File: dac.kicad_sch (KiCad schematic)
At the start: 29 parts, among them U6 PCM5242RHBR, X1 22.5792Mhz, X2 24.576Mhz

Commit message: Page settings
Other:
- company: (none) -> github.com/pedalboard
- title: (none) -> Open Pedalboard Soundcard
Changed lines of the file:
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@@
 (kicad_sch (version 20230121) (generator eeschema)
   (paper "A4")
+  (title_block
+    (title "Open Pedalboard Soundcard")
+    (date "2023-12-19")
+    (rev "0.0.1")
+    (company "github.com/pedalboard")
+    (comment 1 "Source Code: https://github.com/pedalboard/pedalboard-hw")
+    (comment 2 "License: CERN Open Hardware Licence Version 2 - Permissive")
+  )
   (junction (at 99.06 73.66) (diameter 0) (color 0 0 0 0)
   )

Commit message: Distribute parts on PCB
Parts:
- added J2: Conn_02x03_Odd_Even, Connector_PinHeader_2.54mm:PinHeader_2x03_P2.54mm_Vertical, symbol Connector_Generic:Conn_02x03_Odd_Even
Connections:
- net GND: now also J2.3 (Pin_3), J2.4 (Pin_4)
- net outl+: now also J2.6 (Pin_6)
- net outl-: now also J2.5 (Pin_5)
- net outr+: now also J2.2 (Pin_2)
- net outr-: now also J2.1 (Pin_1)
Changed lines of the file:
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@@
+    (stroke (width 0) (type default))
+  )
+  (wire (pts (xy 59.69 139.7) (xy 53.34 139.7))
     (stroke (width 0) (type default))
   )
@@
     (stroke (width 0) (type default))
   )
-  (wire (pts (xy 45.72 137.16) (xy 46.99 137.16))
+  (wire (pts (xy 144.78 156.21) (xy 138.43 156.21))
+    (stroke (width 0) (type default))
+  )
+  (wire (pts (xy 39.37 137.16) (xy 46.99 137.16))
     (stroke (width 0) (type default))
   )
@@
     (stroke (width 0) (type default))
   )
+  (wire (pts (xy 144.78 161.29) (xy 138.43 161.29))
+    (stroke (width 0) (type default))
+  )
   (wire (pts (xy 238.76 76.2) (xy 238.76 73.66))
     (stroke (width 0) (type default))
@@
     (stroke (width 0) (type default))
   )
+  (wire (pts (xy 113.03 158.75) (xy 125.73 158.75))
+    (stroke (width 0) (type default))
+  )
   (wire (pts (xy 71.12 161.29) (xy 77.47 161.29))
     (stroke (width 0) (type default))
@@
     (stroke (width 0) (type default))
   )
-  (wire (pts (xy 72.39 139.7) (xy 71.12 139.7))
-    (stroke (width 0) (type default))
-  )
   (wire (pts (xy 204.47 85.09) (xy 204.47 81.28))
     (stroke (width 0) (type default))
@@
     (stroke (width 0) (type default))
   )
-  (wire (pts (xy 78.74 137.16) (xy 77.47 137.16))
+  (wire (pts (xy 86.36 137.16) (xy 77.47 137.16))
     (stroke (width 0) (type default))
   )
@@
     (stroke (width 0) (type default))
   )
+  (wire (pts (xy 119.38 156.21) (xy 125.73 156.21))
+    (stroke (width 0) (type default))
+  )
   (wire (pts (xy 85.09 105.41) (xy 102.87 105.41))
     (stroke (width 0) (type default))
@@
     (stroke (width 0) (type default))
   )
-  (wire (pts (xy 52.07 139.7) (xy 53.34 139.7))
-    (stroke (width 0) (type default))
-  )
   (wire (pts (xy 148.59 100.33) (xy 170.18 100.33))
     (stroke (width 0) (type default))
@@
     (stroke (width 0) (type default))
   )
+  (wire (pts (xy 138.43 158.75) (xy 151.13 158.75))
+    (stroke (width 0) (type default))
+  )
+  (wire (pts (xy 64.77 139.7) (xy 71.12 139.7))
+    (stroke (width 0) (type default))
+  )
   (wire (pts (xy 191.77 92.71) (xy 191.77 102.87))
     (stroke (width 0) (type default))
@@
     (stroke (width 0) (type default))
   )
+  (wire (pts (xy 119.38 161.29) (xy 125.73 161.29))
+    (stroke (width 0) (type default))
+  )
   (wire (pts (xy 53.34 161.29) (xy 53.34 154.94))
     (stroke (width 0) (type default))
@@
   (wire (pts (xy 182.88 102.87) (xy 182.88 110.49))
     (stroke (width 0) (type default))
+  )
+  (label "outl-" (at 59.69 139.7 180) (fields_autoplaced)
+    (effects (font (size 1.27 1.27)) (justify right bottom))
+  )
+  (label "outl+" (at 144.78 161.29 180) (fields_autoplaced)
+    (effects (font (size 1.27 1.27)) (justify right bottom))
+  )
+  (label "outl-" (at 119.38 161.29 0) (fields_autoplaced)
+    (effects (font (size 1.27 1.27)) (justify left bottom))
+  )
+  (label "outr+" (at 86.36 137.16 180) (fields_autoplaced)
+    (effects (font (size 1.27 1.27)) (justify right bottom))
+  )
+  (label "outr-" (at 119.38 156.21 0) (fields_autoplaced)
+    (effects (font (size 1.27 1.27)) (justify left bottom))
+  )
+  (label "outr+" (at 144.78 156.21 180) (fields_autoplaced)
+    (effects (font (size 1.27 1.27)) (justify right bottom))
+  )
+  (label "outl+" (at 39.37 137.16 0) (fields_autoplaced)
+    (effects (font (size 1.27 1.27)) (justify left bottom))
+  )
+  (label "outr-" (at 64.77 139.7 0) (fields_autoplaced)
+    (effects (font (size 1.27 1.27)) (justify left bottom))
   )
   (global_label "DVDD" (shape input) (at 95.25 73.66 180)
@@
     )
   )
-  (global_label "outr+" (shape input) (at 78.74 137.16 0)
-    (effects (font (size 1.27 1.27)) (justify left))
-    (property "Intersheetrefs" "${INTERSHEET_REFS}" (at 78.74 137.16 0)
-      (effects (font (size 1.27 1.27)) hide)
-    )
-  )
   (global_label "DIN" (shape input) (at 148.59 97.79 0)
     (effects (font (size 1.27 1.27)) (justify left))
     (property "Intersheetrefs" "${INTERSHEET_REFS}" (at 148.59 97.79 0)
-      (effects (font (size 1.27 1.27)) hide)
-    )
-  )
-  (global_label "outr-" (shape input) (at 72.39 139.7 0)
-    (effects (font (size 1.27 1.27)) (justify left))
-    (property "Intersheetrefs" "${INTERSHEET_REFS}" (at 72.39 139.7 0)
       (effects (font (size 1.27 1.27)) hide)
     )
@@
     )
   )
-  (global_label "outl-" (shape input) (at 52.07 139.7 180)
-    (effects (font (size 1.27 1.27)) (justify right))
-    (property "Intersheetrefs" "${INTERSHEET_REFS}" (at 52.07 139.7 0)
-      (effects (font (size 1.27 1.27)) hide)
-    )
-  )
   (global_label "AVDD" (shape input) (at 86.36 118.11 180)
     (effects (font (size 1.27 1.27)) (justify right))
     (property "Intersheetrefs" "${INTERSHEET_REFS}" (at 86.36 118.11 0)
-      (effects (font (size 1.27 1.27)) hide)
-    )
-  )
-  (global_label "outl+" (shape input) (at 45.72 137.16 180)
-    (effects (font (size 1.27 1.27)) (justify right))
-    (property "Intersheetrefs" "${INTERSHEET_REFS}" (at 45.72 137.16 0)
       (effects (font (size 1.27 1.27)) hide)
     )
@@
     )
   )
+  (symbol (lib_id "power:GND") (at 151.13 158.75 0) (unit 1)
+    (in_bom yes) (on_board yes) (dnp no) (fields_autoplaced)
+    (property "Reference" "#PWR017" (at 151.13 165.1 0)
+      (effects (font (size 1.27 1.27)) hide)
+    )
+    (property "Value" "GND" (at 151.13 163.83 0)
+      (effects (font (size 1.27 1.27)))
+    )
+    (property "Footprint" "" (at 151.13 158.75 0)
+      (effects (font (size 1.27 1.27)) hide)
+    )
+    (property "Datasheet" "" (at 151.13 158.75 0)
+      (effects (font (size 1.27 1.27)) hide)
+    )
+    (pin "1")
+    (instances
+      (project "pedalboard-soundcard"
+        (path "/257597c6-fbef-4478-b0f4-968f2d6f1866/c0100554-f979-4e8d-b08c-e48cc1e12bdc"
+          (reference "#PWR017") (unit 1)
+        )
+      )
+    )
+  )
+  (symbol (lib_id "power:GND") (at 113.03 158.75 0) (unit 1)
+    (in_bom yes) (on_board yes) (dnp no) (fields_autoplaced)
+    (property "Reference" "#PWR016" (at 113.03 165.1 0)
+      (effects (font (size 1.27 1.27)) hide)
+    )
+    (property "Value" "GND" (at 113.03 163.83 0)
+      (effects (font (size 1.27 1.27)))
+    )
+    (property "Footprint" "" (at 113.03 158.75 0)
+      (effects (font (size 1.27 1.27)) hide)
+    )
+    (property "Datasheet" "" (at 113.03 158.75 0)
+      (effects (font (size 1.27 1.27)) hide)
+    )
+    (pin "1")
+    (instances
+      (project "pedalboard-soundcard"
+        (path "/257597c6-fbef-4478-b0f4-968f2d6f1866/c0100554-f979-4e8d-b08c-e48cc1e12bdc"
+          (reference "#PWR016") (unit 1)
+        )
+      )
+    )
+  )
   (symbol (lib_id "power:GND") (at 152.4 83.82 0) (unit 1)
     (in_bom yes) (on_board yes) (dnp no)
@@
       (effects (font (size 1.524 1.524)) hide)
     )
-    (property "Datasheet" "" (at 102.87 85.09 0)
+    (property "Datasheet" "https://www.ti.com/lit/ds/symlink/pcm5242.pdf" (at 85.09 44.45 0)
       (effects (font (size 1.524 1.524)))
     )
@@
         )
       )
+    )
+  )
+  (symbol (lib_id "Connector_Generic:Conn_02x03_Odd_Even") (at 130.81 158.75 0) (unit 1)
+    (in_bom yes) (on_board yes) (dnp no) (fields_autoplaced)
+    (property "Reference" "J2" (at 132.08 149.86 0)
+      (effects (font (size 1.27 1.27)))
+    )
+    (property "Value" "Conn_02x03_Odd_Even" (at 132.08 152.4 0)
+      (effects (font (size 1.27 1.27)))
+    )
+    (property "Footprint" "Connector_PinHeader_2.54mm:PinHeader_2x03_P2.54mm_Vertical" (at 130.81 158.75 0)
+      (effects (font (size 1.27 1.27)) hide)
+    )
+    (property "Datasheet" "~" (at 130.81 158.75 0)
+      (effects (font (size 1.27 1.27)) hide)
+    )
+    (pin "1")
+    (pin "2")
+    (pin "3")
+    (pin "4")
+    (pin "5")
+    (pin "6")
+    (instances
+      (project "pedalboard-soundcard"
+        (path "/257597c6-fbef-4478-b0f4-968f2d6f1866/c0100554-f979-4e8d-b08c-e48cc1e12bdc"
+          (reference "J2") (unit 1)
+        )
+      )

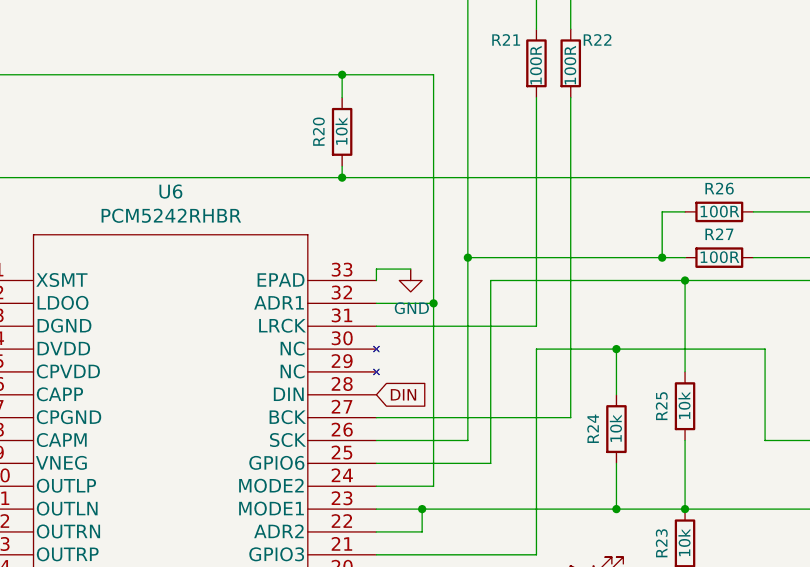
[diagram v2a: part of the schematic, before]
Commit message: First routing attempt
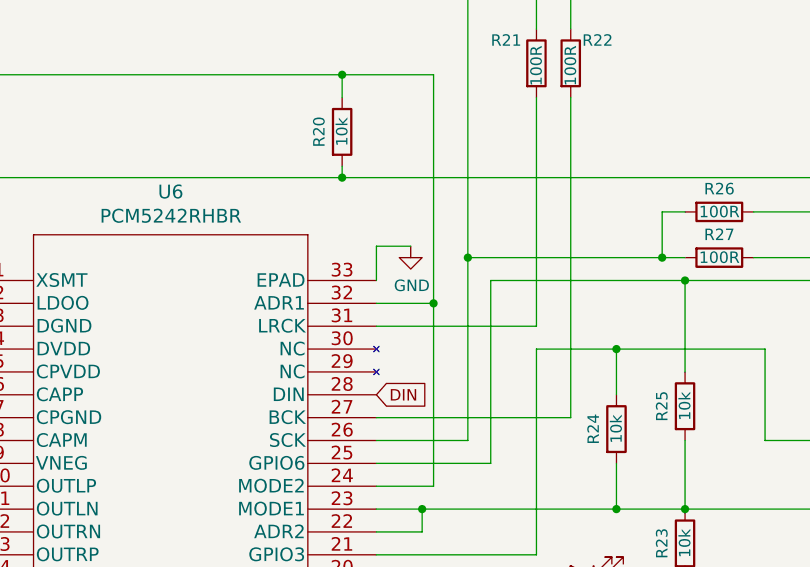
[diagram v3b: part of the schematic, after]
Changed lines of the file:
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@@
     (stroke (width 0) (type default))
   )
-  (wire (pts (xy 148.59 83.82) (xy 148.59 85.09))
+  (wire (pts (xy 148.59 81.28) (xy 148.59 85.09))
     (stroke (width 0) (type default))
   )
@@
     (stroke (width 0) (type default))
   )
-  (wire (pts (xy 148.59 83.82) (xy 152.4 83.82))
+  (wire (pts (xy 148.59 81.28) (xy 152.4 81.28))
     (stroke (width 0) (type default))
   )
@@
     )
   )
-  (symbol (lib_id "power:GND") (at 152.4 83.82 0) (unit 1)
-    (in_bom yes) (on_board yes) (dnp no)
-    (property "Reference" "#PWR016" (at 152.4 90.17 0)
-      (effects (font (size 1.27 1.27)) hide)
-    )
-    (property "Value" "GND" (at 152.527 88.2142 0)
-      (effects (font (size 1.27 1.27)))
-    )
-    (property "Footprint" "" (at 152.4 83.82 0)
-      (effects (font (size 1.27 1.27)) hide)
-    )
-    (property "Datasheet" "" (at 152.4 83.82 0)
-      (effects (font (size 1.27 1.27)) hide)
-    )
+  (symbol (lib_id "power:GND") (at 152.4 81.28 0) (unit 1)
+    (in_bom yes) (on_board yes) (dnp no)
+    (property "Reference" "#PWR016" (at 152.4 87.63 0)
+      (effects (font (size 1.27 1.27)) hide)
+    )
+    (property "Value" "GND" (at 152.527 85.6742 0)
+      (effects (font (size 1.27 1.27)))
+    )
+    (property "Footprint" "" (at 152.4 81.28 0)
+      (effects (font (size 1.27 1.27)) hide)
+    )
+    (property "Datasheet" "" (at 152.4 81.28 0)
+      (effects (font (size 1.27 1.27)) hide)
+    )

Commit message: Cleanup routing
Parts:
- U6: footprint pedalboard-soundcard:PCM5242RHBR -> Package_DFN_QFN:HVQFN-32-1EP_5x5mm_P0.5mm_EP3.1x3.1mm_ThermalVias
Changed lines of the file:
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@@
       (effects (font (size 1.524 1.524)))
     )
-    (property "Footprint" "pedalboard-soundcard:PCM5242RHBR" (at 125.73 78.994 0)
+    (property "Footprint" "Package_DFN_QFN:HVQFN-32-1EP_5x5mm_P0.5mm_EP3.1x3.1mm_ThermalVias" (at 125.73 78.994 0)
       (effects (font (size 1.524 1.524)) hide)
     )

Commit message: Improve 3d model
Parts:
- U6: footprint Package_DFN_QFN:HVQFN-32-1EP_5x5mm_P0.5mm_EP3.1x3.1mm_ThermalVias -> pedalboard-soundcard:HVQFN-32-1EP_5x5mm_P0.5mm_EP3.1x3.1mm_ThermalVias
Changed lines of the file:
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@@
       (effects (font (size 1.524 1.524)))
     )
-    (property "Footprint" "Package_DFN_QFN:HVQFN-32-1EP_5x5mm_P0.5mm_EP3.1x3.1mm_ThermalVias" (at 125.73 78.994 0)
+    (property "Footprint" "pedalboard-soundcard:HVQFN-32-1EP_5x5mm_P0.5mm_EP3.1x3.1mm_ThermalVias" (at 125.73 78.994 0)
       (effects (font (size 1.524 1.524)) hide)
     )

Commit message: Improve 3d models (XTAL)
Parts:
- X1, X2: footprint Oscillator:Oscillator_SMD_Abracon_ASDMB-4Pin_2.5x2.0mm -> pedalboard-soundcard:Oscillator_SMD_Abracon_ASDMB-4Pin_2.5x2.0mm
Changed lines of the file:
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@@
       (effects (font (size 1.27 1.27)) (justify left))
     )
-    (property "Footprint" "Oscillator:Oscillator_SMD_Abracon_ASDMB-4Pin_2.5x2.0mm" (at 236.22 111.76 0)
+    (property "Footprint" "pedalboard-soundcard:Oscillator_SMD_Abracon_ASDMB-4Pin_2.5x2.0mm" (at 236.22 111.76 0)
       (effects (font (size 1.27 1.27)) hide)
     )
@@
       (effects (font (size 1.27 1.27)) (justify left))
     )
-    (property "Footprint" "Oscillator:Oscillator_SMD_Abracon_ASDMB-4Pin_2.5x2.0mm" (at 217.17 90.17 0)
-      (effects (font (size 1.27 1.27)) hide)
-    )
+    (property "Footprint" "pedalboard-soundcard:Oscillator_SMD_Abracon_ASDMB-4Pin_2.5x2.0mm" (at 217.17 90.17 0)
+      (effects (font (size 1.27 1.27)) hide)
+    )

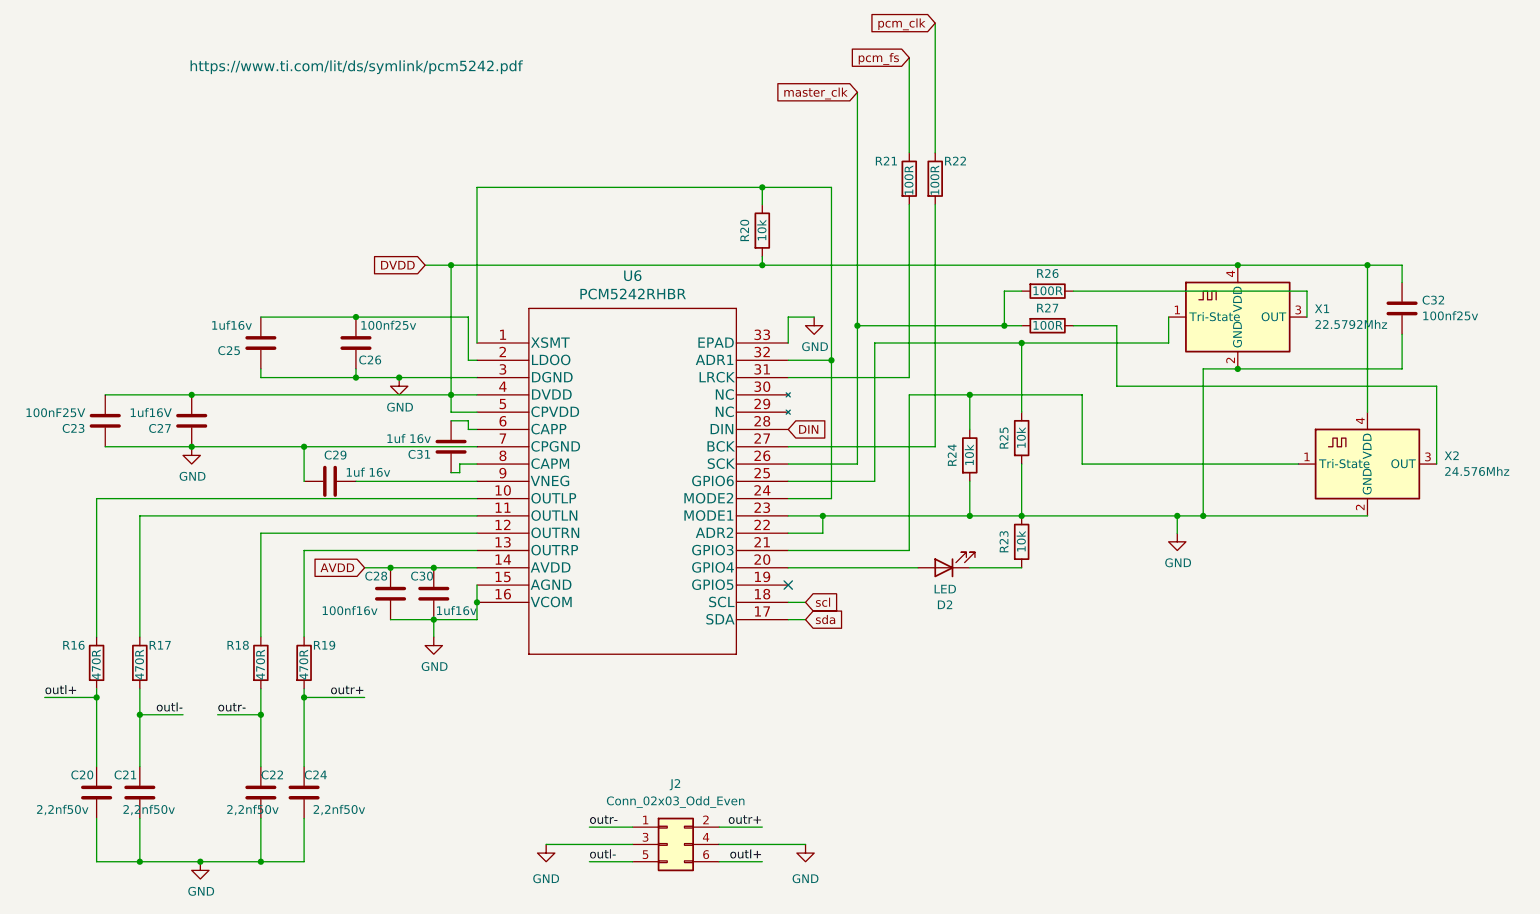
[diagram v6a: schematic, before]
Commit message: improve BOM
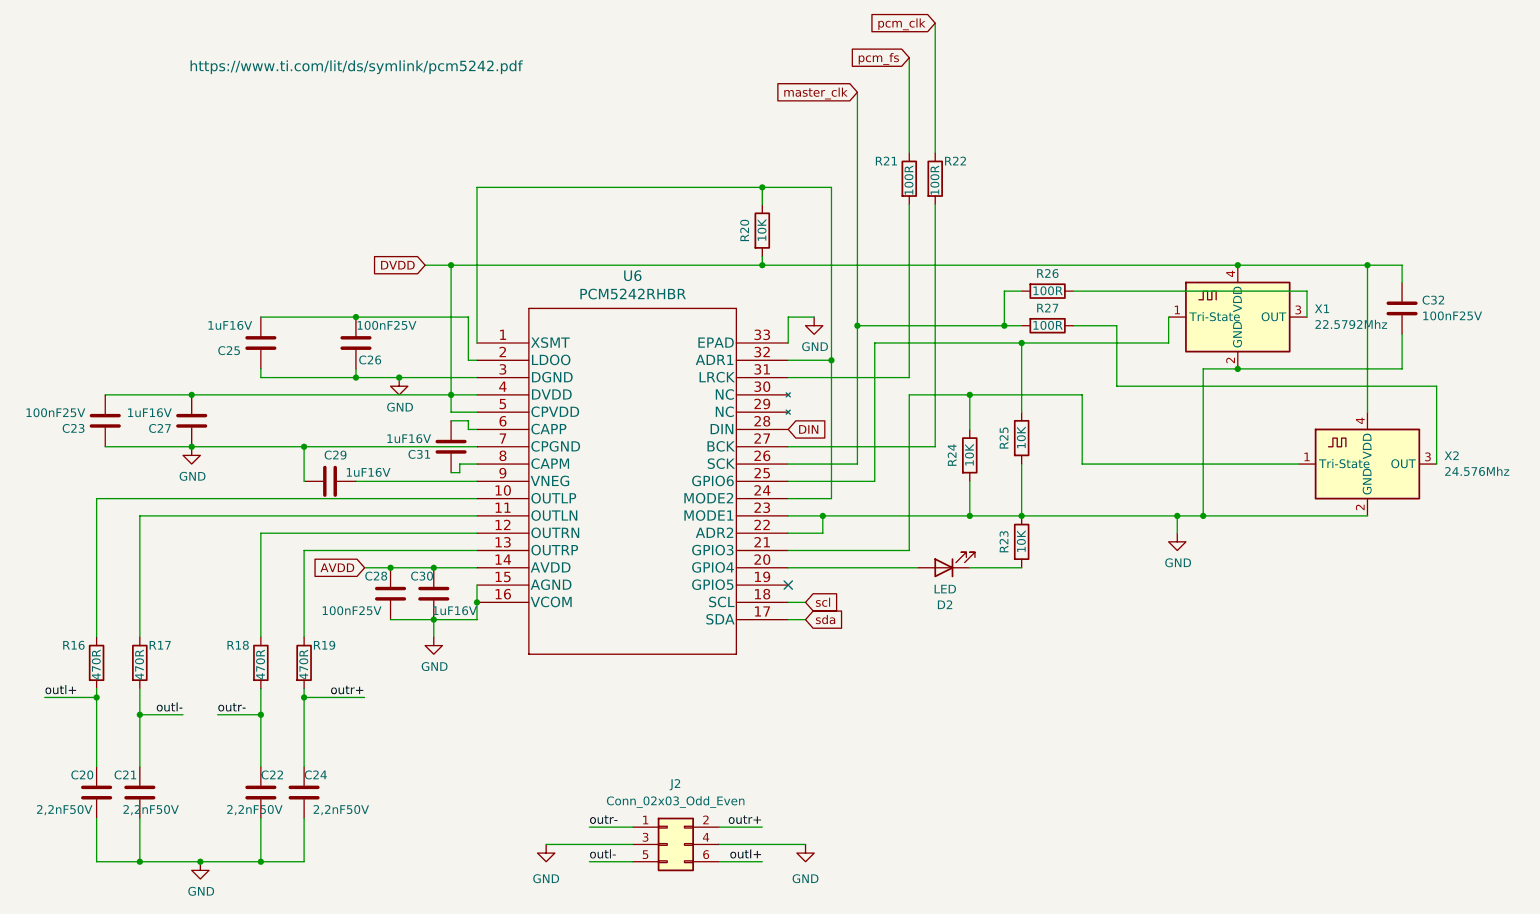
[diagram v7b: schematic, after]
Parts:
- C20, C21, C22, C24: value 2,2nf50v -> 2,2nF50V; Supplier (none) -> https://www.digikey.ch/de/products/detail/samsung-electro-m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
- C23: Supplier (none) -> https://www.digikey.ch/de/products/detail/samsung-electro-m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
- C25, C30: value 1uf16v -> 1uF16V; Supplier (none) -> https://www.digikey.ch/de/products/detail/samsung-electro-m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
- C26, C32: value 100nf25v -> 100nF25V; Supplier (none) -> https://www.digikey.ch/de/products/detail/samsung-electro-m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
- C27: value 1uf16V -> 1uF16V; Supplier (none) -> https://www.digikey.ch/de/products/detail/samsung-electro-m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
- C28: value 100nf16v -> 100nF25V; Supplier (none) -> https://www.digikey.ch/de/products/detail/samsung-electro-m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
- C29, C31: value 1uf 16v -> 1uF16V; Supplier (none) -> https://www.digikey.ch/de/products/detail/samsung-electro-m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
- R16, R17, R18, R19, R21, R22, R26, R27: Supplier (none) -> https://www.digikey.ch/de/products/detail/stackpole-electro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
- R20, R23, R24, R25: value 10k -> 10K; Supplier (none) -> https://www.digikey.ch/de/products/detail/stackpole-electro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
- U6: Supplier (none) -> https://www.digikey.ch/de/products/detail/texas-instruments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
- X1: Supplier (none) -> https://www.digikey.ch/de/products/detail/abracon-llc/ASV-2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
- X2: Supplier (none) -> https://www.digikey.ch/de/products/detail/abracon-llc/ASDMB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
